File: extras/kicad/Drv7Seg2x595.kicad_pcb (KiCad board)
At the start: 2 copper layers, 67.3 x 50.8 mm, 33 parts, among them IC1 74HC595, IC2 74HC595, Q1 MMBT3904, Q2 MMBT3904, Q3 MMBT3904, Q4 MMBT3904

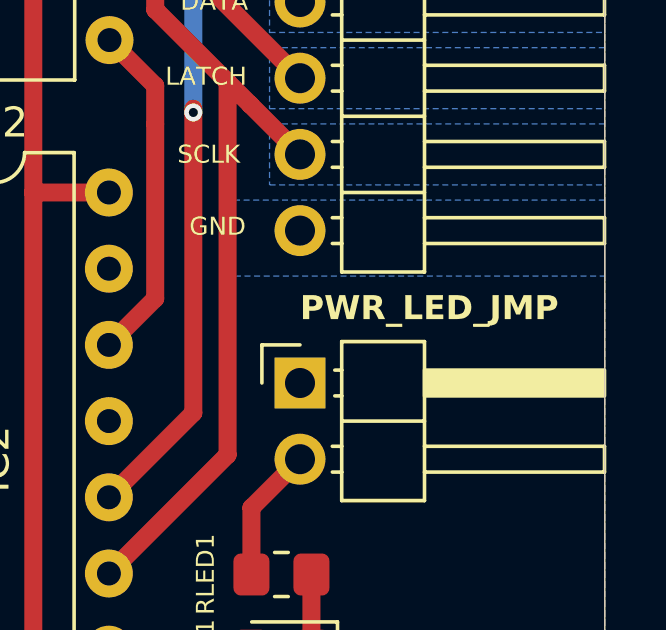
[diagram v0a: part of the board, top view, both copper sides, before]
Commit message: Reworking the KiCAD symbols.
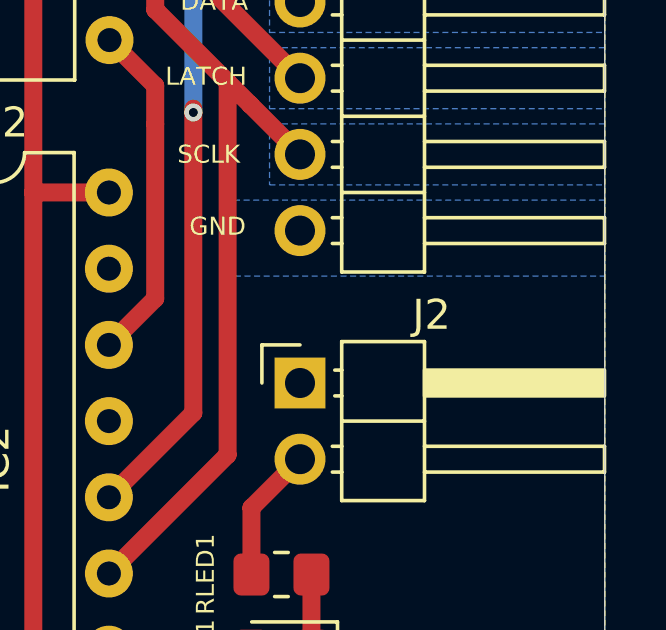
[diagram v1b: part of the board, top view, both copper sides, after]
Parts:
- J2: renamed from Header2; value pin_header_1-row_2-pin_horizontal -> PWR_LED_JMP
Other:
- board text removed: "PWR_LED_JMP"
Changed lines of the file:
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@@
 		(descr "Through hole angled pin header, 1x02, 2.54mm pitch, 6mm pin length, single row")
 		(tags "Through hole angled pin header THT 1x02 2.54mm single row")
-		(property "Reference" "Header2"
+		(property "Reference" "J2"
 			(at 4.385 -2.27 0)
 			(layer "F.SilkS")
-			(hide yes)
 			(effects
 				(font
@@
 			)
 		)
-		(property "Value" "pin_header_1-row_2-pin_horizontal"
+		(property "Value" "PWR_LED_JMP"
 			(at 4.385 4.81 0)
 			(layer "F.Fab")
-			(hide yes)
 			(effects
 				(font
@@
 			)
 		)
-		(property "Datasheet" "~"
+		(property "Datasheet" ""
 			(at 0 0 0)
 			(layer "F.Fab")
@@
 			)
 		)
-		(property "Description" "Pin header, single row, 2 pins"
+		(property "Description" ""
 			(at 0 0 0)
 			(layer "F.Fab")
@@
 			)
 			(justify left bottom)
-		)
-	)
-	(gr_text "PWR_LED_JMP"
-		(at 173.99 100.838 0)
-		(layer "F.SilkS")
-		(effects
-			(font
-				(size 0.8 0.8)
-				(thickness 0.15)
-				(bold yes)
-			)
-			(justify left bottom)

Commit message: Major update of KiCAD files.
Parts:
- removed Header1: pin_header_1-row_5-pin_horizontal, Connector_PinHeader_2.54mm:PinHeader_1x05_P2.54mm_Horizontal
- removed LED1: LED, LED_SMD:LED_0805_2012Metric_Pad1.15x1.40mm_HandSolder
- added D1: LED1, LED_SMD:LED_0805_2012Metric_Pad1.15x1.40mm_HandSolder, F.Cu at (173.2, 111.8)
- added J1: INTERFACE, Connector_PinHeader_2.54mm:PinHeader_1x05_P2.54mm_Horizontal, F.Cu at (174.0, 87.6)
- DISPLAY1: value 7seg_4d -> display_7seg_4d
- J2: footprint Connector_PinHeader_2.54mm:PinHeader_1x02_P2.54mm_Horizontal -> Drv7Seg2x595:PinHeader_1x02_P2.54mm_Horizontal
- Q1, Q2, Q3, Q4: footprint Package_TO_SOT_SMD:SOT-23_Handsoldering -> Package_TO_SOT_SMD:SOT-23
- RT1, RT2, RT3, RT4: value 150 -> 1k5
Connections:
- J2 pad 1: GND -> Net-(J2-Pin_1)
- J2 pad 2: Net-(Header2-Pin_2) -> GND
- RLED1 pad 1: Net-(Header2-Pin_2) -> Net-(J2-Pin_1)
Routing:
- net Net-(J2-Pin_1): track 0.00 -> 4.55 mm
- net Net-(Header2-Pin_2): track 4.55 -> 0.00 mm
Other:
- board size 67.3 x 50.8 mm -> 67.4 x 50.8 mm
- board text removed: "INTERFACE"

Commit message: Update KiCAD files.
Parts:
- DISPLAY1: footprint Display_7Segment:CA56-12EWA -> Drv7Seg2x595:display_7seg_4d_0.56in
- J1: footprint Connector_PinHeader_2.54mm:PinHeader_1x05_P2.54mm_Horizontal -> Drv7Seg2x595:PinHeader_1x05_P2.54mm_Horizontal

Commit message: Add SOT-23 to project-wide library for portability.
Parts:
- Q1, Q2, Q3, Q4: footprint Package_TO_SOT_SMD:SOT-23 -> Drv7Seg2x595:SOT-23

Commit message: Increase RLED1 value to 680 Ohm.
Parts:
- RLED1: value 330 -> 680
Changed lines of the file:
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@@
 			)
 		)
-		(property "Value" "330"
+		(property "Value" "680"
 			(at 0 1.65 0)
 			(layer "F.Fab")

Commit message: Bump BJT base pull-down resistors values to 47k.
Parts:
- RTPD1, RTPD2, RTPD3, RTPD4: value 1k5 -> 47k
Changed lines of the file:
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@@
 			)
 		)
-		(property "Value" "1k5"
+		(property "Value" "47k"
 			(at 0 1.65 0)
 			(layer "F.Fab")
@@
 			)
 		)
-		(property "Value" "1k5"
+		(property "Value" "47k"
 			(at 0 1.65 0)
 			(layer "F.Fab")
@@
 			)
 		)
-		(property "Value" "1k5"
+		(property "Value" "47k"
 			(at 0 1.65 0)
 			(layer "F.Fab")
@@
 			)
 		)
-		(property ki_fp_filters "*CA56*12EWA*")
 		(sheetname "/")
 		(sheetfile "Drv7Seg2x595.kicad_sch")
@@
 			)
 		)
-		(property "Value" "1k5"
+		(property "Value" "47k"
 			(at 0 1.65 0)
 			(layer "F.Fab")
